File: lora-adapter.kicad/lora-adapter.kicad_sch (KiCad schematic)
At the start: 6 parts, among them J1 Conn_LoRa, U1 RFM9x_Lora_Breakout

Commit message: LoRa-adapter: Rev 1.00 ready for production
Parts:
- U1: now left out of the parts list
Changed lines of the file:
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@@
   (title_block
     (title "LoRa-Adapter")
-    (date "2023-12-03")
-    (rev "0.9")
+    (date "2023-12-07")
+    (rev "1.0")
     (company "Bernhard Bablok")
     (comment 1 "https://github.com/bablokb/pcb-pico-datalogger")
@@
   )
   (symbol (lib_id "user:RFM9x_Lora_Breakout") (at 110.236 52.07 0) (unit 1)
-    (in_bom yes) (on_board yes)
+    (in_bom no) (on_board yes)
     (property "Reference" "U1" (id 0) (at 115.824 29.21 0))
     (property "Value" "RFM9x_Lora_Breakout" (id 1) (at 115.824 32.258 0))

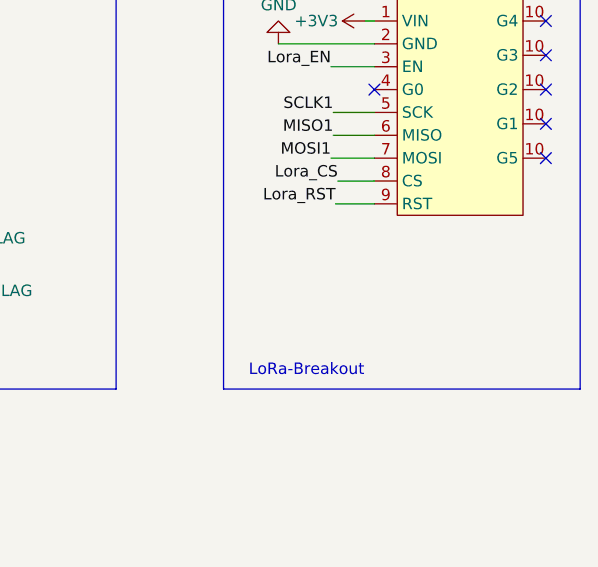
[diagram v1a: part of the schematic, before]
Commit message: LoRa-Adaper Rev 1.10: add pin-sockets to board (and production files)
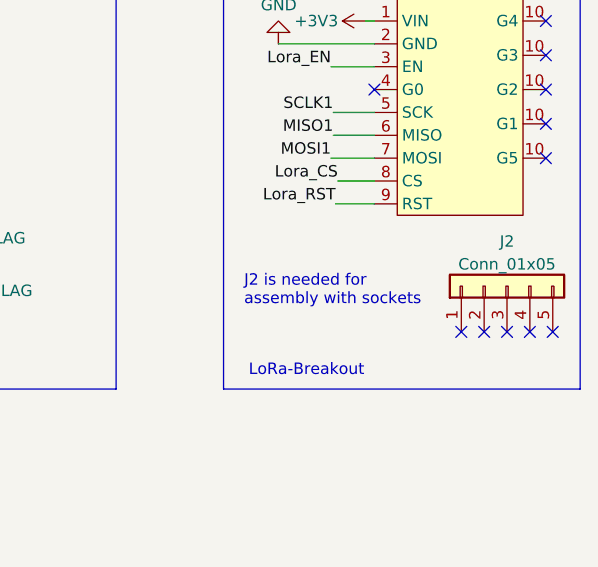
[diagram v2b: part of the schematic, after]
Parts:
- added J2: Conn_01x05, Connector_PinSocket_2.54mm:PinSocket_1x05_P2.54mm_Vertical, symbol Connector_Generic:Conn_01x05
- U1: footprint user:RFM9x_Lora_Breakout -> Connector_PinSocket_2.54mm:PinSocket_1x09_P2.54mm_Vertical; LCSC (none) -> C2897372; now in the parts list
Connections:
- no-connect marks 6 -> 11
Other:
- note added: "J2 is needed for assembly with sockets"
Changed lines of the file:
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@@
   (title_block
     (title "LoRa-Adapter")
-    (date "2023-12-07")
-    (rev "1.0")
+    (date "2024-01-10")
+    (rev "1.10")
     (company "Bernhard Bablok")
     (comment 1 "https://github.com/bablokb/pcb-pico-datalogger")
@@
   (no_connect (at 125.476 36.83))
   (no_connect (at 125.476 44.45))
+  (no_connect (at 118.618 71.374))
+  (no_connect (at 123.698 71.374))
   (no_connect (at 106.426 44.45))
+  (no_connect (at 126.238 71.374))
+  (no_connect (at 116.078 71.374))
   (no_connect (at 125.476 52.07))
   (no_connect (at 125.476 48.26))
   (no_connect (at 125.476 40.64))
+  (no_connect (at 121.158 71.374))
   (wire (pts (xy 53.34 53.594) (xy 49.276 53.594))
     (stroke (width 0) (type default) (color 0 0 0 0))
@@
     )
   )
+  (text "J2 is needed for\nassembly with sockets" (at 91.948 68.58 0)
+    (effects (font (size 1.27 1.27)) (justify left bottom))
+  )
   (text "LoRa-Breakout" (at 92.456 76.454 0)
     (effects (font (size 1.27 1.27)) (justify left bottom))
@@
   )
   (symbol (lib_id "user:RFM9x_Lora_Breakout") (at 110.236 52.07 0) (unit 1)
-    (in_bom no) (on_board yes)
+    (in_bom yes) (on_board yes)
     (property "Reference" "U1" (id 0) (at 115.824 29.21 0))
     (property "Value" "RFM9x_Lora_Breakout" (id 1) (at 115.824 32.258 0))
-    (property "Footprint" "user:RFM9x_Lora_Breakout" (id 2) (at 116.586 63.5 0)
+    (property "Footprint" "Connector_PinSocket_2.54mm:PinSocket_1x09_P2.54mm_Vertical" (id 2) (at 116.586 63.5 0)
       (effects (font (size 1.27 1.27)) hide)
     )
     (property "Datasheet" "" (id 3) (at 110.236 52.07 0)
+      (effects (font (size 1.27 1.27)) hide)
+    )
+    (property "LCSC" "C2897372" (id 4) (at 110.236 52.07 0)
       (effects (font (size 1.27 1.27)) hide)
     )
@@
     (pin "9")
   )
+  (symbol (lib_id "Connector_Generic:Conn_01x05") (at 121.158 66.294 90) (unit 1)
+    (in_bom yes) (on_board yes) (fields_autoplaced)
+    (property "Reference" "J2" (id 0) (at 121.158 61.3242 90))
+    (property "Value" "Conn_01x05" (id 1) (at 121.158 63.8611 90))
+    (property "Footprint" "Connector_PinSocket_2.54mm:PinSocket_1x05_P2.54mm_Vertical" (id 2) (at 121.158 66.294 0)
+      (effects (font (size 1.27 1.27)) hide)
+    )
+    (property "Datasheet" "~" (id 3) (at 121.158 66.294 0)
+      (effects (font (size 1.27 1.27)) hide)
+    )
+    (property "LCSC" "C2897368" (id 4) (at 121.158 66.294 0)
+      (effects (font (size 1.27 1.27)) hide)
+    )
+    (pin "1")
+    (pin "2")
+    (pin "3")
+    (pin "4")
+    (pin "5")
+  )
   (symbol (lib_id "Mechanical:MountingHole") (at 55.626 185.166 0) (unit 1)
     (in_bom no) (on_board yes) (fields_autoplaced)
@@
       (reference "J1") (unit 1) (value "Conn_LoRa") (footprint "Connector_JST:JST_SUR_BM08B-SURS-TF_1x08-1MP_P0.80mm_Vertical")
     )
+    (path "/302007b9-8360-4c6d-9786-e52fd8a9d813"
+      (reference "J2") (unit 1) (value "Conn_01x05") (footprint "Connector_PinSocket_2.54mm:PinSocket_1x05_P2.54mm_Vertical")
+    )
     (path "/29bc2c23-53af-49b8-8082-04cb9cb85643"
-      (reference "U1") (unit 1) (value "RFM9x_Lora_Breakout") (footprint "user:RFM9x_Lora_Breakout")
-    )
-  )
+      (reference "U1") (unit 1) (value "RFM9x_Lora_Breakout") (footprint "Connector_PinSocket_2.54mm:PinSocket_1x09_P2.54mm_Vertical")
+    )
+  )
